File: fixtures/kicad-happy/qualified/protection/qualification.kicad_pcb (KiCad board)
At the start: 2 copper layers, 8 parts, among them J1 USB_B, J2 Power, U1 LM317, U2 Load

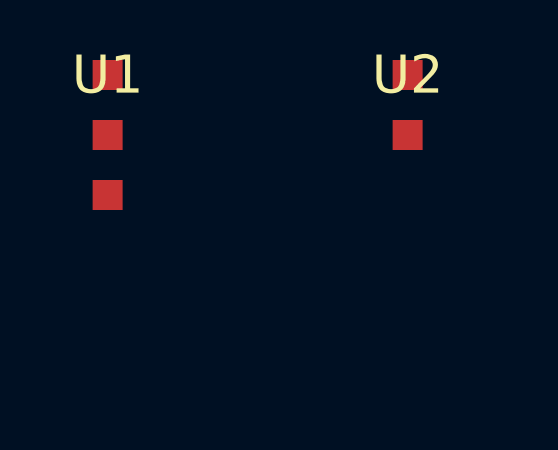
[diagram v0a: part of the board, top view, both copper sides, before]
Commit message: Qualify derating, thermal and EMC adapters with source-backed boundary evidence
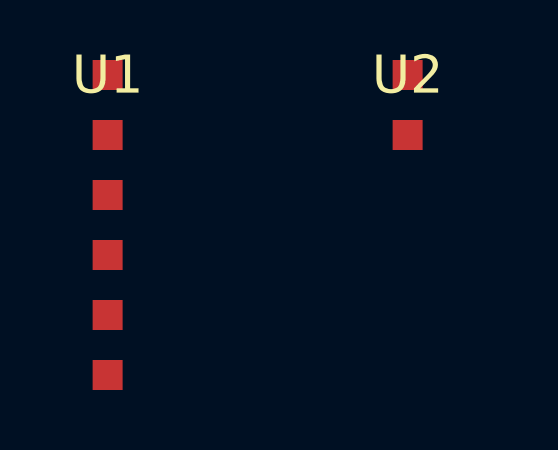
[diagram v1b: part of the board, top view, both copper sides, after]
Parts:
- R1: value 720 -> 379
- R2: value 240 -> 121
- U1: value LM317 -> TPS7A4501
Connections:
- U1 pad 2: +5V -> +12V
- U1 pad 3: FB -> GND
